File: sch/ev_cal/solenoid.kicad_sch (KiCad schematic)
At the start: 5 parts, among them J12 Conn_01x01_Female, Q1 AO3434A

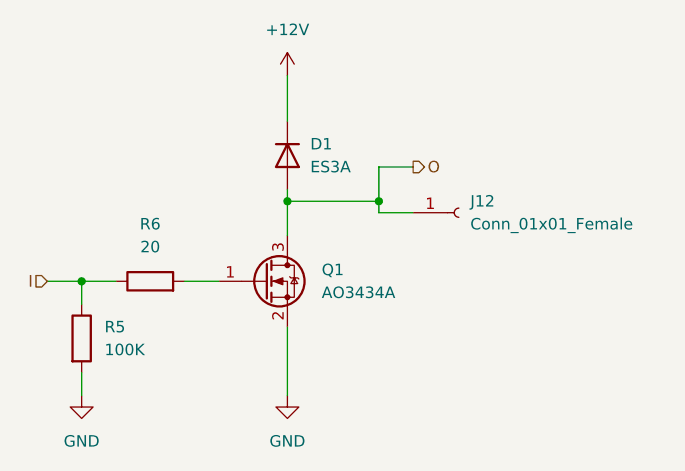
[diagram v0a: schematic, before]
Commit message: Added PDF of schematic
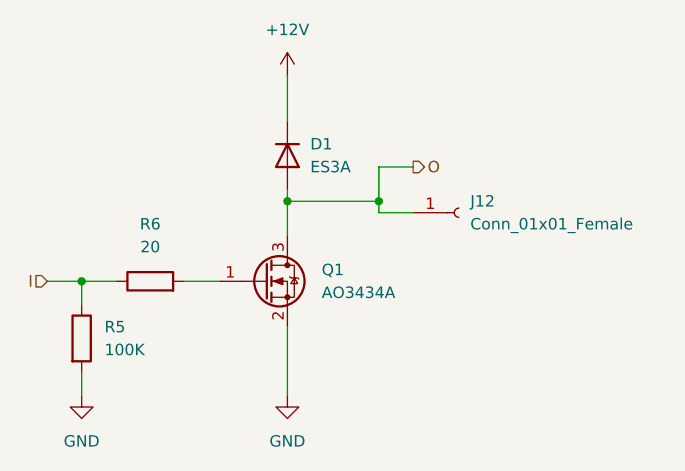
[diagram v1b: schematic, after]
